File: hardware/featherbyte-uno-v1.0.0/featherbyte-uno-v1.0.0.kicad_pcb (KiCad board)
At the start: 2 copper layers, 54 x 60 mm, 63 parts, among them J1 Conn_01x08, J10 Conn_01x09, J2 Conn_01x10, J3 Conn_01x06, J5 USB_C_Receptacle_16P, J6 SWD Connector, J7 Terminal Block, J8 USB_C_Receptacle_16P, J9 BOOT1, SW1 Reset, SW2 BOOT0, SW3 SW_DIP_x04, U1 CH32V203CxT6, U2 TJA1050, U4 AMS1117-3.3, U5 USBLC6-2P6, U6 USBLC6-2P6, Y1 8M, Y3 32.768K

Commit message: drc check process ongoing
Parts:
- moved C14 0.15 mm to (87.1, 82.9)
- moved C12 0.15 mm to (88.2, 81.8)
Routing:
- net GND: track 6.90 -> 23.1 mm, vias 92 -> 79
- net +3.3V: track 190.0 -> 196.2 mm, vias 10 -> 12
- net /USBH_D+: track 5.11 -> 8.06 mm
- net +5V: track 84.9 -> 82.0 mm
- net /USBH_D-: track 5.11 -> 7.11 mm
- net /D4: track 32.5 -> 34.1 mm
- net Net-(J5-CC2): track 14.2 -> 13.4 mm
- net /CAN0TX: track 22.3 -> 21.7 mm
- net /D9: track 35.6 -> 36.1 mm
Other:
- rule pad_to_mask_clearance: 0.2032 -> 0
- rule solder_mask_min_width: 0.2032 -> 0.1524

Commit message: pin labeling and drc checks has been done
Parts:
- moved J6 2.05 mm to (74.7, 70.5)
- moved R16 0.56 mm to (99.7, 57.3)
- moved R15 0.56 mm to (99.7, 63.0)
- moved R6 0.51 mm to (99.7, 61.2)
- moved R5 0.47 mm to (99.7, 59.2)
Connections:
- J2 pad 3: unconnected-(J2-Pin_3-Pad3) -> GND
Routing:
- net GND: track 23.1 -> 114.7 mm, vias 79 -> 269
- net +5V: track 82.0 -> 95.3 mm
- net +3.3V: track 196.2 -> 186.1 mm, vias 12 -> 9
- net /SWCLK: track 18.7 -> 21.4 mm
- net /SWDIO: track 28.5 -> 31.1 mm
- net /NRST: track 83.4 -> 85.1 mm
- net /VBUS2: track 33.4 -> 34.3 mm
- net VBUS: track 41.8 -> 41.0 mm
- net /OSC_OUT: track 14.2 -> 13.5 mm
- net /VBUS1: track 33.9 -> 34.5 mm
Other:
- board text added: "3.3V"
- board text added: "5V"
- board text added: "A0"
- board text added: "A1"
- board text added: "A2"
- board text added: "A3"
- board text added: "A4/SDA"
- board text added: "A5/SCL"
- board text added: "A6"
- board text added: "BOOT0"
- board text added: "BOOT1"
- board text added: "CAN-H"
- board text added: "D0"
- board text added: "D1"
- board text added: "D10"
- board text added: "D11"
- board text added: "D12"
- board text added: "D13"
- board text added: "D2"
- board text added: "D3"
- board text added: "D4"
- board text added: "D5"
- board text added: "D6"
- board text added: "D7"
- board text added: "D8"
- board text added: "D9"
- board text added: "GND"
- board text added: "IOREF"
- board text added: "RESET"
- board text added: "RST"
- board text added: "SCL"
- board text added: "SDA"

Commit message: pcb ready
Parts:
- added G***: LOGO, featherbyte-uno-v1.0.0:logo, F.Cu at (174.4, 81.9)
- added REF**: OSHW-Logo2_7.3x6mm_SilkScreen, Symbol:OSHW-Logo2_7.3x6mm_SilkScreen, F.Cu at (146.6, 109.4)
- moved D3 63.7 mm to (136.5, 63.5), turned to 0 degrees
- moved C13 62.7 mm to (153.4, 97.1)
- moved C14 62.7 mm to (149.6, 88.6)
- moved C17 62.7 mm to (163.1, 77.4)
- moved C3 62.7 mm to (163.1, 79.9)
- moved C5 62.7 mm to (150.4, 78.7)
- moved C8 62.7 mm to (148.4, 90.9)
- moved C9 62.7 mm to (147.1, 92.3)
- moved J7 62.7 mm to (156.1, 117.3)
- moved R10 62.7 mm to (145.6, 87.8)
- moved R16 62.7 mm to (162.2, 63.0)
- moved R5 62.7 mm to (162.2, 65.0)
- moved REF** 62.7 mm to (138.3, 119.0)
- moved C10 62.7 mm to (164.2, 90.6)
- moved C12 62.7 mm to (150.7, 87.5)
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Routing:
- net +3.3V: track 186.1 -> 190.6 mm
- net Net-(J5-CC1): track 13.3 -> 16.4 mm
- net GND: track 114.7 -> 117.7 mm, vias 269 -> 258
- net Net-(D3-A): track 1.76 -> 3.29 mm
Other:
- board text added: "0"
- board text added: "1"
- board text added: "CAN-L"
- board text added: "CC1"
- board text added: "CC2"
- board text added: "NRST"
- board text added: "SWCLK"
- board text added: "SWDIO"
- board text added: "USB1"
- board text added: "USB2"
- board text removed: "CAN-H"

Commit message: version info addition and adc pin correction done
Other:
- board text added: "A4"
- board text added: "A5"
- board text added: "V1.0.0"
- board text removed: "A4/SDA"
- board text removed: "A5/SCL"
- board text removed: "A6"
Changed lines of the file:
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@@
 	)
 	(footprint "Resistor_SMD:R_0603_1608Metric"
+		(locked yes)
 		(layer "F.Cu")
 		(at 168.35 114.815 -90)
@@
 	)
 	(footprint "Capacitor_SMD:C_0603_1608Metric"
+		(locked yes)
 		(layer "F.Cu")
 		(at 142.469796 98.709796 -45)
@@
 	)
 	(footprint "TestPoint:TestPoint_Pad_D1.5mm"
+		(locked yes)
 		(layer "F.Cu")
 		(at 148.725 75.015 90)
@@
 	)
 	(footprint "TestPoint:TestPoint_Pad_D1.5mm"
+		(locked yes)
 		(layer "F.Cu")
 		(at 159.25 72.515)
@@
 	)
 	(footprint "Package_SO:SO-8_3.9x4.9mm_P1.27mm"
+		(locked yes)
 		(layer "F.Cu")
 		(at 159.525 106.315 -90)
@@
 	)
 	(footprint "Resistor_SMD:R_0603_1608Metric"
+		(locked yes)
 		(layer "F.Cu")
 		(at 162.15 68.79)
@@
 		(property "Reference" "REF**"
 			(at 0.23 4.36 0)
-			(layer "F.SilkS")
+			(layer "Cmts.User")
 			(effects
 				(font
@@
 	)
 	(footprint "Capacitor_SMD:C_0603_1608Metric"
+		(locked yes)
 		(layer "F.Cu")
 		(at 166.7 114.815 90)
@@
 	)
 	(footprint "Connector_PinHeader_2.54mm:PinHeader_2x03_P2.54mm_Vertical"
+		(locked yes)
 		(layer "F.Cu")
 		(at 137.125 76.275)
@@
 	)
 	(footprint "Resistor_SMD:R_0603_1608Metric"
+		(locked yes)
 		(layer "F.Cu")
 		(at 163.1 106.84 90)
@@
 	)
 	(footprint "Crystal:Crystal_SMD_HC49-SD"
+		(locked yes)
 		(layer "F.Cu")
 		(at 146.594796 97.609796 -45)
@@
 		(property "Reference" "REF**"
 			(at -3.89 -0.14 90)
-			(layer "F.SilkS")
+			(layer "Cmts.User")
 			(effects
 				(font
@@
 	)
 	(footprint "Capacitor_SMD:C_0603_1608Metric"
-		(locked yes)
 		(layer "F.Cu")
 		(at 153.425 97.065 -135)
@@
 	)
 	(footprint "Resistor_SMD:R_0603_1608Metric"
+		(locked yes)
 		(layer "F.Cu")
 		(at 180.15 63.79)
@@
 	)
 	(footprint "Resistor_SMD:R_0603_1608Metric"
+		(locked yes)
 		(layer "F.Cu")
 		(at 162.175 64.965)
@@
 	)
 	(footprint "Resistor_SMD:R_0603_1608Metric"
+		(locked yes)
 		(layer "F.Cu")
 		(at 180.125 65.39)
@@
 	)
 	(footprint "LED_SMD:LED_0805_2012Metric"
+		(locked yes)
 		(layer "F.Cu")
 		(at 136.5 63.515)
@@
 	)
 	(footprint "featherbyte-uno-v1.0.0:logo"
+		(locked yes)
 		(layer "F.Cu")
 		(at 174.45 81.94 -90)
 		(property "Reference" "G***"
 			(at 3.075 -14.95 90)
-			(layer "F.SilkS")
+			(layer "Cmts.User")
 			(effects
 				(font
@@
 	)
 	(footprint "Resistor_SMD:R_0603_1608Metric"
+		(locked yes)
 		(layer "F.Cu")
 		(at 134.575 65.465)
@@
 	)
 	(footprint "Resistor_SMD:R_0603_1608Metric"
+		(locked yes)
 		(layer "F.Cu")
 		(at 162.15 66.94)
@@
 	)
 	(footprint "Capacitor_SMD:C_0603_1608Metric"
+		(locked yes)
 		(layer "F.Cu")
 		(at 145.294796 101.509796 135)
@@
 		(property "Reference" "REF**"
 			(at 0.63 4.06 0)
-			(layer "F.SilkS")
+			(layer "Cmts.User")
 			(effects
 				(font
@@
 	)
 	(footprint "Resistor_SMD:R_0603_1608Metric"
+		(locked yes)
 		(layer "F.Cu")
 		(at 162.175 63.015)
@@
 	)
 	(footprint "Capacitor_SMD:C_0603_1608Metric"
+		(locked yes)
 		(layer "F.Cu")
 		(at 155.95 106.99 90)
@@
 	)
 	(footprint "Crystal:Crystal_SMD_3215-2Pin_3.2x1.5mm"
+		(locked yes)
 		(layer "F.Cu")
 		(at 149.6 93.615 45)
@@
 		(tags "Through hole socket strip THT 1x08 2.54mm single row")
 		(property "Reference" "J1"
-			(at 0 -2.8 180)
+			(at -1.1 -2 180)
 			(layer "F.SilkS")
 			(effects
@@
 	)
 	(footprint "Capacitor_SMD:C_0603_1608Metric"
+		(locked yes)
 		(layer "F.Cu")
 		(at 147.05 92.265 135)
@@
 	)
 	(footprint "Capacitor_SMD:C_0603_1608Metric"
+		(locked yes)
 		(layer "F.Cu")
 		(at 148.425 90.89 135)
@@
 		)
 	)
-	(gr_text "A6"
-		(at 135 103.715 0)
+	(gr_text "A0"
+		(at 135.075 104.318571 0)
 		(layer "F.SilkS")
 		(effects
@@
 		)
 	)
-	(gr_text "A5/SCL"
-		(at 135 105.910238 0)
+	(gr_text "A1"
+		(at 135.075 106.852857 0)
 		(layer "F.SilkS")
 		(effects
@@
 		)
 	)
-	(gr_text "A4/SDA"
-		(at 135 108.105476 0)
+	(gr_text "A2"
+		(at 135.075 109.387143 0)
 		(layer "F.SilkS")
 		(effects
@@
 	)
 	(gr_text "A3"
-		(at 135 110.300715 0)
-		(layer "F.SilkS")
-		(effects
-			(font
-				(size 1 1)
-				(thickness 0.2)
-				(bold yes)
-			)
-			(justify left bottom)
-		)
-	)
-	(gr_text "A2"
-		(at 135 112.495953 0)
+		(at 135.075 111.921428 0)
 		(layer "F.SilkS")
 		(effects
@@
 		)
 	)
-	(gr_text "A1"
-		(at 135 114.691191 0)
+	(gr_text "A4"
+		(at 135.075 114.455714 0)
 		(layer "F.SilkS")
 		(effects
@@
 		)
 	)
-	(gr_text "A0"
-		(at 135 116.886429 0)
+	(gr_text "A5"
+		(at 135.075 116.99 0)
 		(layer "F.SilkS")
 		(effects
@@
 			)
 		)
+	)
+	(gr_text "V1.0.0"
+		(at 181.2 120.615 0)
+		(layer "F.SilkS")
+		(effects
+			(font
+				(size 1 1)
+				(thickness 0.2032)
+				(bold yes)
+			)
+		)

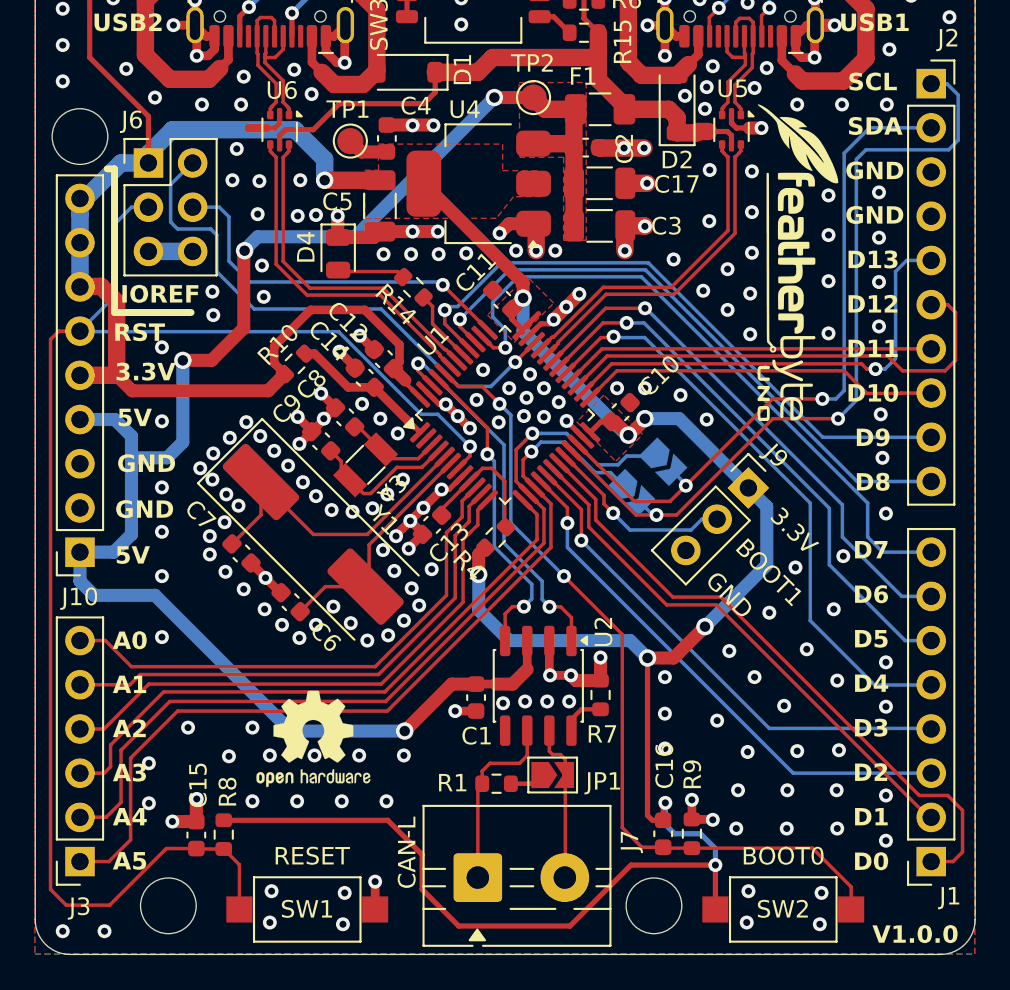
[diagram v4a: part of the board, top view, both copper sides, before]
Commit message: actual mcu pin names added to back silk screen layer
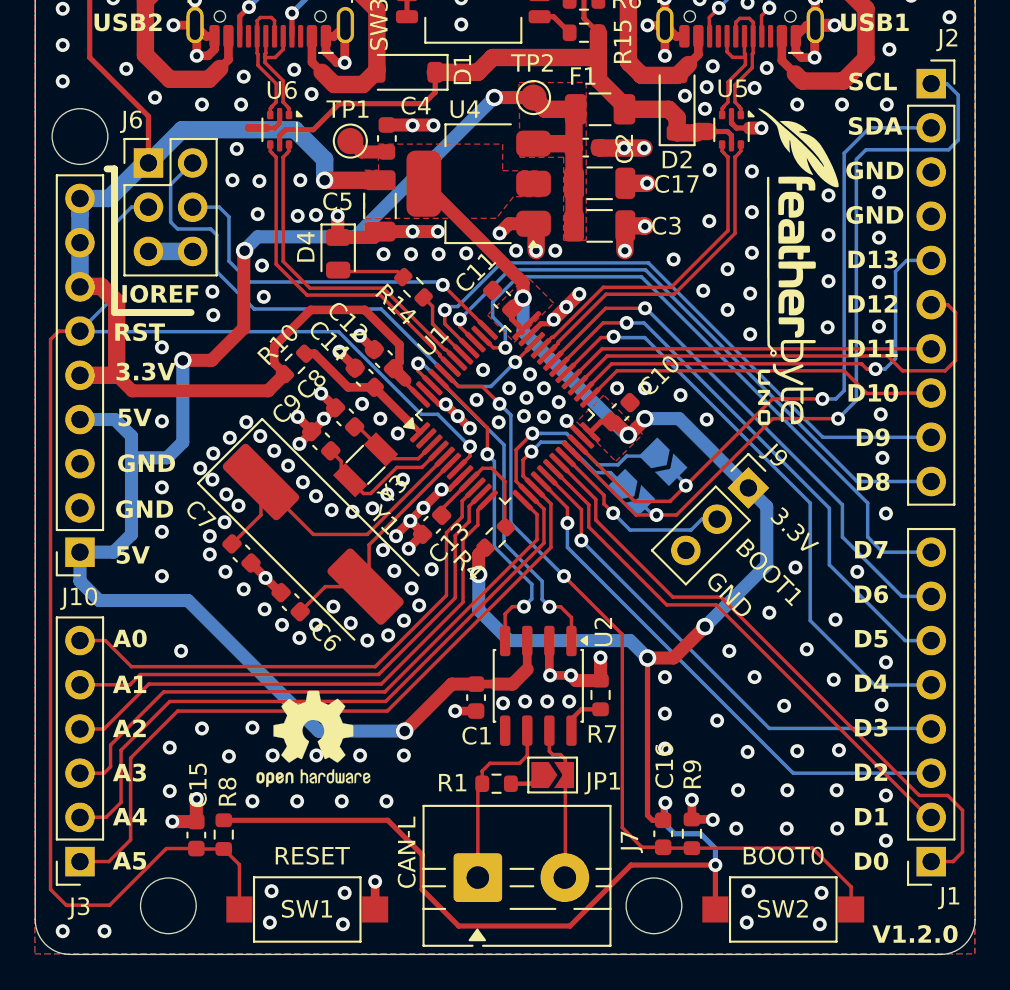
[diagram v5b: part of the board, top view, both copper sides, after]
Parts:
- removed the G*** at (174.4, 81.9)
- added G***: LOGO, footprints:logo, F.Cu at (174.5, 82.2)
- J6: value SWD Connector -> Conn_02x03
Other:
- board text added: "PA0"
- board text added: "PA1"
- board text added: "PA10"
- board text added: "PA15"
- board text added: "PA2"
- board text added: "PA3"
- board text added: "PA4"
- board text added: "PA5"
- board text added: "PA6"
- board text added: "PA7"
- board text added: "PA8"
- board text added: "PA9"
- board text added: "PB0"
- board text added: "PB1"
- board text added: "PB10"
- board text added: "PB11"
- board text added: "PB12"
- board text added: "PB13"
- board text added: "PB14"
- board text added: "PB15"
- board text added: "PB3"
- board text added: "PB4"
- board text added: "V1.2.0"
- board text removed: "V1.0.0"
